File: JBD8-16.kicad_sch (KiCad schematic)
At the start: 57 parts, among them J1 RS232, J2 5V, SW1 RESET, U1 W65C02SxP, U10 CY62256-70PC(RAM), U11 CY62256-70PC(RAM), U12 CY62256-70PC(RAM), U13 CY62256-70PC(RAM), U14 CY62256-70PC(RAM), U15 CY62256-70PC(RAM), U16 CY62256-70PC(RAM), U17 74LS00, U18 74LS00, U19 74LS11, U20 74LS32, U21 74LS154, U22 74LS11, U23 74LS32, U24 74LS154, U25 74LS08, U26 74LS11, U27 74LS11, U28 74LS32, U29 74LS154, U3 28C256(ROM), U30 74LS08, U31 74LS32, U32 74LS11, U33 74LS32, U34 74LS154, U35 74LS32, U36 74LS08, U37 74LS08, U38 74LS32, U4 6522, U4 CY62256-70PC(RAM), U5 W65C51NxP, U6 MAX232, U7 74LS245, U8 74LS373, U9 74LS138, X1 1Mhz, Y1 1.8432Mhz

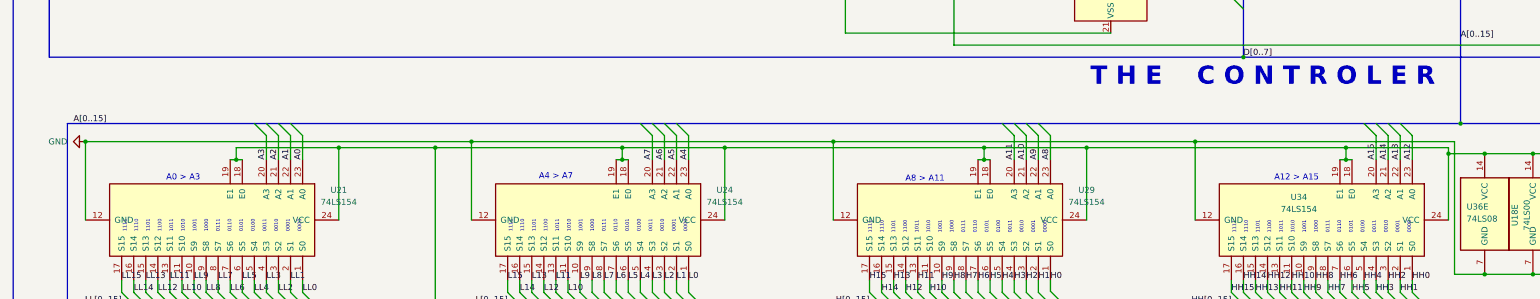
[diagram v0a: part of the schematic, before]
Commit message: Fixed the decoders being inactive
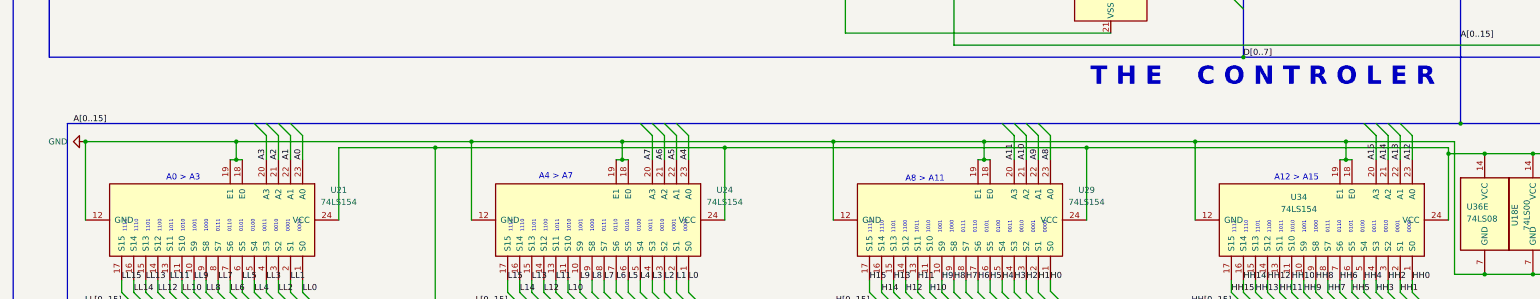
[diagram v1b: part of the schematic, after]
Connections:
- net +5V: no longer U21.18 (E0), U21.19 (E1), U24.18 (E0), U24.19 (E1), U29.18 (E0), U29.19 (E1), U34.18 (E0), U34.19 (E1)
- net GND: now also U21.18 (E0), U21.19 (E1), U24.18 (E0), U24.19 (E1), U29.18 (E0), U29.19 (E1), U34.18 (E0), U34.19 (E1)

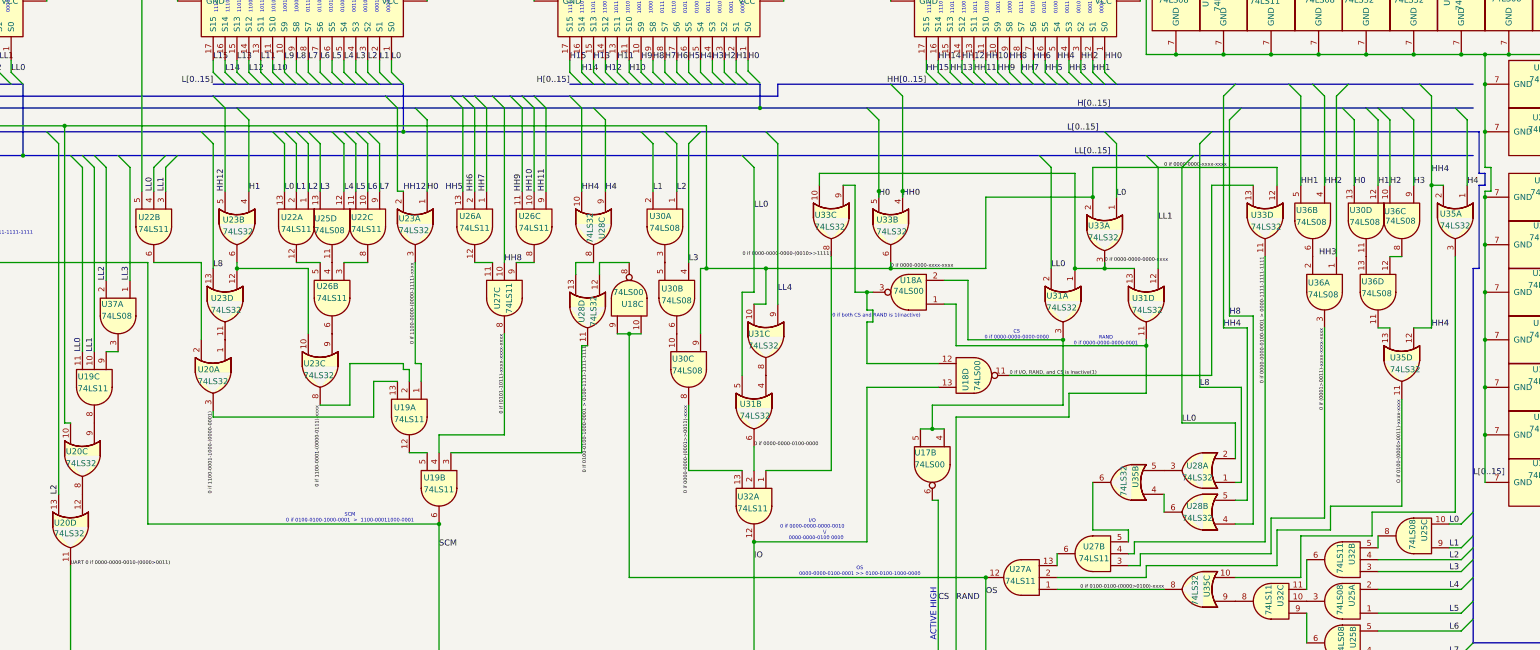
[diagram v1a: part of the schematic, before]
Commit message: Many issues with map which have been labeled
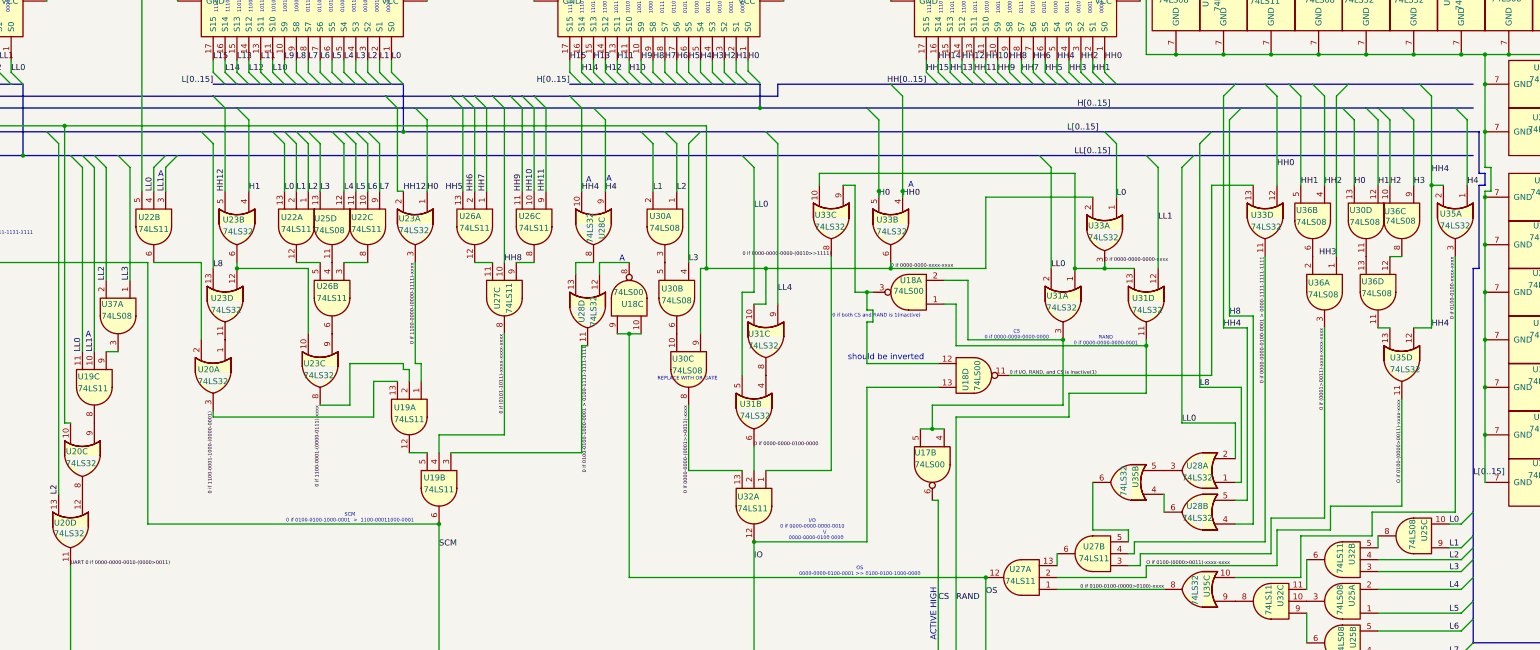
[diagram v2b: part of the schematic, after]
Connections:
- net 0 if 0000-0000-xxxx-xxxx: no longer U19.10, U19.11, U21.1 (S0), U21.2 (S1), U22.3, U22.4, U28.2, U31.12, U31.2, U31.5, U33.12
- net HH0: now also U33.12
- net 0 if 0100-0100-xxxx-xxxx: now reaches U35.10, U35.3
- new net LL0: U19.11, U21.1 (S0), U22.4, U28.2, U31.2, U31.5
- new net LL1: U19.10, U21.2 (S1), U22.3, U31.12
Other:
- note added: "A"
- note added: "REPLACE WITH OR GATE"
- note added: "should be inverted"
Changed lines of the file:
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@@
 	)
 	(junction
+		(at 69.85 591.82)
+		(diameter 0)
+		(color 0 0 0 0)
+	)
+	(junction
 		(at 264.16 424.18)
 		(diameter 0)
@@
 	)
 	(junction
-		(at 69.85 591.82)
-		(diameter 0)
-		(color 0 0 0 0)
-	)
-	(junction
 		(at 431.8 71.12)
 		(diameter 0)
@@
 	)
 	(junction
-		(at 307.34 408.94)
-		(diameter 0)
-		(color 0 0 0 0)
-	)
-	(junction
 		(at 219.71 354.33)
 		(diameter 0)
@@
 	)
 	(bus_entry
+		(at 344.17 384.81)
+		(size 2.54 2.54)
+		(stroke
+			(width 0)
+			(type default)
+		)
+	)
+	(bus_entry
 		(at 309.88 394.97)
 		(size 2.54 2.54)
@@
 		)
 	)
-	(wire
-		(pts
-			(xy 326.39 402.59) (xy 321.31 402.59)
-		)
-		(stroke
-			(width 0)
-			(type default)
-		)
-	)
 	(bus
 		(pts
@@
 	(wire
 		(pts
-			(xy 321.31 402.59) (xy 307.34 402.59)
-		)
-		(stroke
-			(width 0)
-			(type default)
-		)
-	)
-	(wire
-		(pts
 			(xy 364.49 107.95) (xy 364.49 113.03)
 		)
@@
 		)
 	)
-	(wire
-		(pts
-			(xy 346.71 402.59) (xy 326.39 402.59)
-		)
-		(stroke
-			(width 0)
-			(type default)
-		)
-	)
 	(bus
 		(pts
@@
 	(wire
 		(pts
-			(xy 307.34 402.59) (xy 307.34 408.94)
-		)
-		(stroke
-			(width 0)
-			(type default)
-		)
-	)
-	(wire
-		(pts
 			(xy 292.1 35.56) (xy 297.18 35.56)
 		)
@@
 	(bus
 		(pts
-			(xy 337.82 384.81) (xy 349.25 384.81)
+			(xy 337.82 384.81) (xy 344.17 384.81)
 		)
 		(stroke
@@
 		)
 	)
+	(bus
+		(pts
+			(xy 344.17 384.81) (xy 349.25 384.81)
+		)
+		(stroke
+			(width 0)
+			(type default)
+		)
+	)
 	(wire
 		(pts
@@
 	(wire
 		(pts
-			(xy 69.85 591.82) (xy 74.93 591.82)
-		)
-		(stroke
-			(width 0)
-			(type default)
-		)
-	)
-	(wire
-		(pts
 			(xy 280.67 203.2) (xy 281.94 203.2)
 		)
@@
 	(wire
 		(pts
+			(xy 69.85 591.82) (xy 74.93 591.82)
+		)
+		(stroke
+			(width 0)
+			(type default)
+		)
+	)
+	(wire
+		(pts
 			(xy 591.82 228.6) (xy 561.34 228.6)
 		)
@@
 	(wire
 		(pts
-			(xy 346.71 406.4) (xy 346.71 402.59)
+			(xy 346.71 387.35) (xy 346.71 406.4)
 		)
 		(stroke
@@
 		)
 	)
+	(text "REPLACE WITH OR GATE"
+		(exclude_from_sim no)
+		(at 220.726 447.802 0)
+		(effects
+			(font
+				(size 0.762 0.762)
+			)
+		)
+	)
 	(text "ROM\n1100-0001-1000-0010 > 1111-1111-1111-1111"
 		(exclude_from_sim no)
@@
 		)
 	)
+	(text "A"
+		(exclude_from_sim no)
+		(at 268.478 406.4 0)
+		(effects
+			(font
+				(size 1.27 1.27)
+			)
+		)
+	)
 	(text "1111\n\n1110\n\n1101\n\n1100\n\n1011\n\n1010\n\n1001\n\n1000\n\n0111\n\n0110\n\n0101\n\n0100\n\n0011\n\n0010\n\n0001\n\n0000"
 		(exclude_from_sim no)
@@
 		)
 	)
+	(text "A"
+		(exclude_from_sim no)
+		(at 206.756 422.148 0)
+		(effects
+			(font
+				(size 1.27 1.27)
+			)
+		)
+	)
 	(text "A12 > A15"
 		(exclude_from_sim no)
@@
 		)
 	)
+	(text "A"
+		(exclude_from_sim no)
+		(at 108.204 404.114 0)
+		(effects
+			(font
+				(size 1.27 1.27)
+			)
+		)
+	)
 	(text "Only 0 if BANKMEM is selected and a Write is occuring from the CPU"
 		(exclude_from_sim no)
@@
 		)
 	)
+	(text "should be inverted"
+		(exclude_from_sim no)
+		(at 263.144 443.23 0)
+		(effects
+			(font
+				(size 1.27 1.27)
+			)
+		)
+	)
 	(text "THE BANK"
 		(exclude_from_sim no)
@@
 		)
 	)
+	(text "A"
+		(exclude_from_sim no)
+		(at 203.962 405.13 0)
+		(effects
+			(font
+				(size 1.27 1.27)
+			)
+		)
+	)
+	(text "A"
+		(exclude_from_sim no)
+		(at 199.644 405.384 0)
+		(effects
+			(font
+				(size 1.27 1.27)
+			)
+		)
+	)
+	(text "A"
+		(exclude_from_sim no)
+		(at 92.71 438.404 0)
+		(effects
+			(font
+				(size 1.27 1.27)
+			)
+		)
+	)
 	(text "THE BRAINS"
 		(exclude_from_sim no)
@@
 		)
 	)
+	(label "0 if 0100-0100-xxxx-xxxx"
+		(at 384.81 421.64 270)
+		(fields_autoplaced yes)
+		(effects
+			(font
+				(size 0.762 0.762)
+				(color 0 0 0 1)
+			)
+			(justify right bottom)
+		)
+	)
 	(label "A2"
 		(at 269.24 264.16 0)
@@
 		)
 	)
+	(label "O if 0100-(0000>0011)-xxxx-xxxx"
+		(at 318.77 487.68 0)
+		(fields_autoplaced yes)
+		(effects
+			(font
+				(size 0.762 0.762)
+			)
+			(justify left bottom)
+		)
+	)
 	(label "A7"
 		(at 322.58 267.97 0)
@@
 		)
 	)
-	(label "0 if 0000-0000-xxxx-xxxx"
-		(at 322.58 402.59 0)
-		(fields_autoplaced yes)
-		(effects
-			(font
-				(size 0.762 0.762)
-			)
-			(justify left bottom)
-		)
-	)
 	(label "C2"
 		(at 95.25 19.05 0)
@@
 		(effects
 			(font
+				(size 1.27 1.27)
+			)
+			(justify left bottom)
+		)
+	)
+	(label "HH0"
+		(at 346.71 402.59 0)
+		(effects
+			(font

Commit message: Removed unneccasary logic
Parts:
- removed U17: 74LS00, symbol 74xx:74LS00
- removed U32: 74LS11, symbol 74xx:74LS11
- removed U37: 74LS08, symbol 74xx:74LS08
- added U39: 74LS04, symbol 74xx:74LS04
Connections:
- net +5V: now also U39.14 (VCC)
- net 0 if 0000-0000-(0001>>0011)-xxxx: now also U22.13, U38.8; no longer U30.8
- net 0 if 0000-0000-0000-(0010>>1111): now also U22.1
- net 0 if 0000-0000-0100-0000: now also U22.2
- net 0 if 0000-0000-xxxx-xxxx: now also U38.9; no longer U30.9
- net GND: now also U18.10, U18.9, U25.10, U25.9, U39.13, U39.4, U39.7 (GND); no longer U38.10, U38.9
- net IO: now also U22.12
- net L0: now also U25.2; no longer U22.13, U25.10
- net L1: now also U25.5; no longer U22.2, U25.9
- net L2: now also U25.4; no longer U22.1
- net L4: no longer U25.2
- net L5: no longer U25.1
- net L6: no longer U25.5
- net L7: no longer U25.4
- net LL2: now also U30.10
- net LL3: now also U30.9
- net OS: now also U39.9; no longer U18.10, U18.9
- net R~{W}: now also U39.11
- net SCM: now also U39.1
- net ~{R}W: now also U39.10
- net at U26.5: now also U25.3; no longer U22.12
- net at U19.9: now also U30.8
- net at U35.9: now also U23.9, U26.6
- net at U18.2, U31.3: now also U39.3
- net at U18.3, U33.9: now also U39.5; no longer U18.12
- net at U28.12: now also U39.8; no longer U18.8
- net at U20.4: now also U39.2
- net at U30.6: now also U38.10; no longer U30.10
- net at U25.6: now also U25.1
- new net: U18.12, U39.6
- no-connect marks 31 -> 29
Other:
- note removed: "A"
- note removed: "REPLACE WITH OR GATE"
- note removed: "should be inverted"
- moved on the sheet: U18C, U22A, U25A, U25B, U25C, U30C, U38C, U38D

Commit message: Made the physiocal layout of the decoder less stupid
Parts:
- renumbered U33 to U10X, U31 to U11X, U39 to U12X, U30 to U13X, U26 to U14X, U25 to U15X, U22 to U16X, U23 to U17X, U19 to U18X, U20 to U19X, U21 to U1X, U38 to U20X, U24 to U2X, U34 to U4X, U36 to U5X, U35 to U6X, U27 to U7X, U28 to U8X, U18 to U9X
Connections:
- net +5V: now also U7X.11; no longer U16X.5
- net 0 if (0101-1011)-xxxx-xxxx-xxxx: now also U14X.8; no longer U7X.8
- net 0 if 0000-0000-0000-(0010>>1111): now also U11X.11; no longer U10X.8
- net 0 if 0000-0000-0000-xxxx: now also U10X.4; no longer U11X.1
- net 0 if 0000-0000-0100-0001 > 0000-1111-1111-1111: now also U8X.8; no longer U10X.11
- net 0 if 0000-0000-xxxx-xxxx: now also U11X.3; no longer U10X.6
- net 0 if 0100-0100-(0000>0100)-xxxx: now also U8X.3; no longer U6X.8
- net 0 if 0100-0100-xxxx-xxxx: now also U8X.2; no longer U6X.10
- net 0 if 1100-0000-(0000-1111)-xxxx: now also U19X.3; no longer U17X.3
- net 0 if 1100-0001-1000-(0000-0001): now also U17X.3; no longer U19X.3
- net 0 if I/O, RAND, and CS is inactive(1): now also U8X.10, U9X.6; no longer U10X.13, U18.11
- net A14: now also U18.12; no longer U9X.4
- net A15: now also U18.13; no longer U9X.5
- net H0: now also U11X.2, U19X.1; no longer U10X.5, U17X.1
- net H4: now also U10X.12; no longer U8X.9
- net HH0: now also U11X.1, U8X.9; no longer U10X.12, U10X.4
- net HH10: now also U14X.4; no longer U14X.10
- net HH11: now also U14X.3; no longer U14X.9
- net HH12: now also U19X.2; no longer U17X.2
- net HH4: now also U10X.13; no longer U8X.10
- net HH8: now also U14X.10; no longer U7X.10
- net HH9: now also U14X.5; no longer U14X.11
- net IO: now also U9X.5; no longer U18.13
- net L8: now also U6X.9; no longer U8X.1
- net LL0: now also U10X.5, U6X.10, U7X.10; no longer U11X.2, U16X.4, U8X.2
- net LL1: now also U10X.9, U7X.9; no longer U11X.12, U16X.3
- net RAND: now also U10X.8; no longer U11X.11
- net at U16X.8: now also U16X.3; no longer U14X.3
- net at U15X.11: now also U16X.4; no longer U14X.4
- net at U16X.6: now also U17X.9, U8X.1; no longer U19X.2
- net at U17X.11: now also U17X.1; no longer U19X.1
- net at U15X.3: now also U16X.5; no longer U14X.5
- net at U12X.5, U9X.3: now also U11X.12; no longer U10X.9
- net at U12X.6: now also U9X.4; no longer U18.12
- net at U8X.13: now also U10X.11; no longer U8X.8
- net at U12X.3, U9X.2: now also U10X.6; no longer U11X.3
- net at U6X.5: now also U6X.8; no longer U8X.3
- net at U19X.5: now also U18.11; no longer U9X.6
- net at U14X.12: now also U14X.11; no longer U7X.11
- new net: U17X.2, U7X.8
- new net: U14X.6, U14X.9
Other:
- moved on the sheet: U10XB, U10XC, U10XD, U10XE, U11XA, U11XD, U11XE, U12XG, U13XE, U14XB, U14XC, U14XD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

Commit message: THE DECODER WORKSgit add .
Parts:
- renumbered U29 to U3X, U18 to U9X
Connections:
- net GND: no longer U12X.13
- net H4: no longer U10X.12
- net 0 if xxxx-(0000-0011)-xxxx-xxxx: now reaches U5X.11, U6X.13
- net 0 if xxxx-(0000-0011)-xxxx-xxxx: now also U12X.13
- net 1 if xxxx-(0000-0011)-xxxx-xxxx: now reaches U12X.12
- net 1 if xxxx-(0000-0011)-xxxx-xxxx: now also U10X.12
- no-connect marks 29 -> 28
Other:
- note added: "0 if 0100-(0100-1111)-xxxx-xxxx"
- moved on the sheet: U12XF

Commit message: lol
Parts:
- removed U7: 74LS245, symbol 74xx:74LS245
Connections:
- net DD0 is gone; now on net D0: U10.11 (Q0), U11.11 (Q0), U12.11 (Q0), U13.11 (Q0), U14.11 (Q0), U15.11 (Q0), U16.11 (Q0)
- net DD1 is gone; now on net D1: U10.12 (Q1), U11.12 (Q1), U12.12 (Q1), U13.12 (Q1), U14.12 (Q1), U15.12 (Q1), U16.12 (Q1)
- net DD2 is gone; now on net D2: U10.13 (Q2), U11.13 (Q2), U12.13 (Q2), U13.13 (Q2), U14.13 (Q2), U15.13 (Q2), U16.13 (Q2)
- net DD3 is gone; now on net D3: U10.15 (Q3), U11.15 (Q3), U12.15 (Q3), U13.15 (Q3), U14.15 (Q3), U15.15 (Q3), U16.15 (Q3)
- net DD4 is gone; now on net D4: U10.16 (Q4), U11.16 (Q4), U12.16 (Q4), U13.16 (Q4), U14.16 (Q4), U15.16 (Q4), U16.16 (Q4)
- net DD5 is gone; now on net D5: U10.17 (Q5), U11.17 (Q5), U12.17 (Q5), U13.17 (Q5), U14.17 (Q5), U15.17 (Q5), U16.17 (Q5)
- net DD6 is gone; now on net D6: U10.18 (Q6), U11.18 (Q6), U12.18 (Q6), U13.18 (Q6), U14.18 (Q6), U15.18 (Q6), U16.18 (Q6)
- net DD7 is gone; now on net D7: U10.19 (Q7), U11.19 (Q7), U12.19 (Q7), U13.19 (Q7), U14.19 (Q7), U15.19 (Q7), U16.19 (Q7)
- net +5V: now also U9.6 (G1)
- net GND: no longer U9.5 (~{G2B}), U9.6 (G1)
- net R~{W}: now also U1.37 (ϕ0); no longer U1.39 (ϕ2), U10.27 (~{WE}), U11.27 (~{WE}), U12.27 (~{WE}), U13.27 (~{WE}), U14.27 (~{WE}), U15.27 (~{WE}), U16.27 (~{WE}), U20X.6
- net SCM: now also U9.5 (~{G2B})
- new net: U10.27 (~{WE}), U11.27 (~{WE}), U12.27 (~{WE}), U13.27 (~{WE}), U14.27 (~{WE}), U15.27 (~{WE}), U16.27 (~{WE}), U20X.6
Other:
- note added: "Only 0 if SCM is selected and a Write is occuring from the CPU"
- note removed: "Only 0 if BANKMEM is selected and a Write is occuring from the CPU"
- moved on the sheet: U15XC, U20XD, U9XC

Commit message: IT FRICKING WORKS
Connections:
- net L4: now also U11X.9
- net LL4: no longer U11X.9
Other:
- note added: "0110-1001-1010-1111 SCM"
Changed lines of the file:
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@@
 	)
 	(junction
-		(at 55.88 554.99)
-		(diameter 0)
-		(color 0 0 0 0)
-	)
-	(junction
 		(at 506.73 228.6)
 		(diameter 0)
@@
 	)
 	(junction
-		(at 50.8 554.99)
-		(diameter 0)
-		(color 0 0 0 0)
-	)
-	(junction
 		(at 528.32 135.89)
 		(diameter 0)
@@
 	)
 	(junction
+		(at 55.88 554.99)
+		(diameter 0)
+		(color 0 0 0 0)
+	)
+	(junction
 		(at 214.63 219.71)
 		(diameter 0)
@@
 	)
 	(junction
+		(at 50.8 554.99)
+		(diameter 0)
+		(color 0 0 0 0)
+	)
+	(junction
 		(at 416.56 408.94)
 		(diameter 0)
@@
 	(wire
 		(pts
-			(xy 50.8 554.99) (xy 55.88 554.99)
-		)
-		(stroke
-			(width 0)
-			(type default)
-		)
-	)
-	(wire
-		(pts
 			(xy 312.42 50.8) (xy 317.5 50.8)
 		)
@@
 		)
 	)
+	(bus
+		(pts
+			(xy 388.62 424.18) (xy 388.62 504.19)
+		)
+		(stroke
+			(width 0)
+			(type default)
+		)
+	)
 	(wire
 		(pts
@@
 	(wire
 		(pts
-			(xy 364.49 440.69) (xy 364.49 502.92)
-		)
-		(stroke
-			(width 0)
-			(type default)
-		)
-	)
-	(wire
-		(pts
 			(xy 459.74 261.62) (xy 497.84 261.62)
 		)
@@
 	(wire
 		(pts
+			(xy 364.49 440.69) (xy 364.49 502.92)
+		)
+		(stroke
+			(width 0)
+			(type default)
+		)
+	)
+	(wire
+		(pts
 			(xy 214.63 224.79) (xy 214.63 229.87)
 		)
@@
 		)
 	)
-	(bus
-		(pts
-			(xy 388.62 424.18) (xy 388.62 504.19)
-		)
-		(stroke
-			(width 0)
-			(type default)
-		)
-	)
 	(wire
 		(pts
@@
 	(wire
 		(pts
+			(xy 50.8 554.99) (xy 55.88 554.99)
+		)
+		(stroke
+			(width 0)
+			(type default)
+		)
+	)
+	(wire
+		(pts
 			(xy 299.72 485.14) (xy 299.72 487.68)
 		)
@@
 		)
 	)
+	(text "0110-1001-1010-1111 SCM"
+		(exclude_from_sim no)
+		(at 301.752 461.518 0)
+		(effects
+			(font
+				(size 1.27 1.27)
+			)
+		)
+	)
 	(text "ACTIVE HIGH"
 		(exclude_from_sim no)
@@
 		)
 	)
+	(label "R~{W}"
+		(at 463.55 223.52 0)
+		(fields_autoplaced yes)
+		(effects
+			(font
+				(size 1.27 1.27)
+				(thickness 0.254)
+				(bold yes)
+			)
+			(justify left bottom)
+		)
+	)
 	(label "H10"
 		(at 208.28 382.27 0)
@@
 		)
 	)
-	(label "LL4"
+	(label "L4"
 		(at 240.03 429.26 0)
 		(fields_autoplaced yes)
